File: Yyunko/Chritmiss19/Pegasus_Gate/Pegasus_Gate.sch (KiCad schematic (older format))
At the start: 38 parts, among them J1 Conn_01x03_Female, J2 Conn_01x03_Female, U1 WS2811, U2 WS2811, U3 WS2811, U4 1528-1537-ND

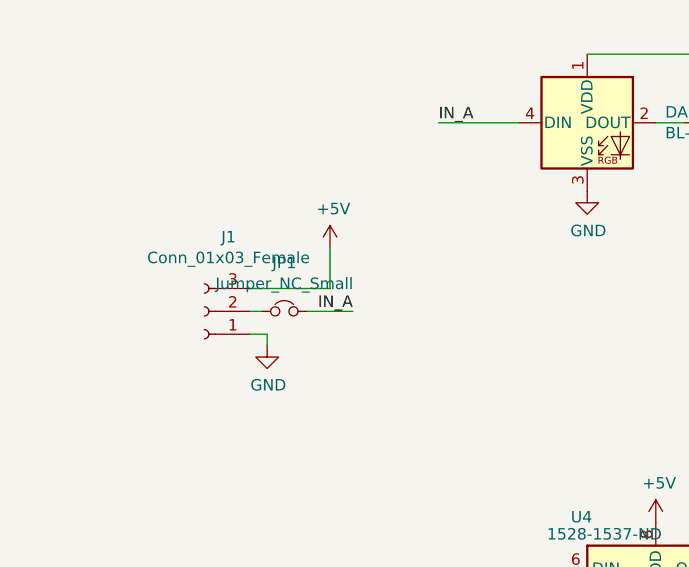
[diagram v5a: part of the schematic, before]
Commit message: Begin work on ESP32 code
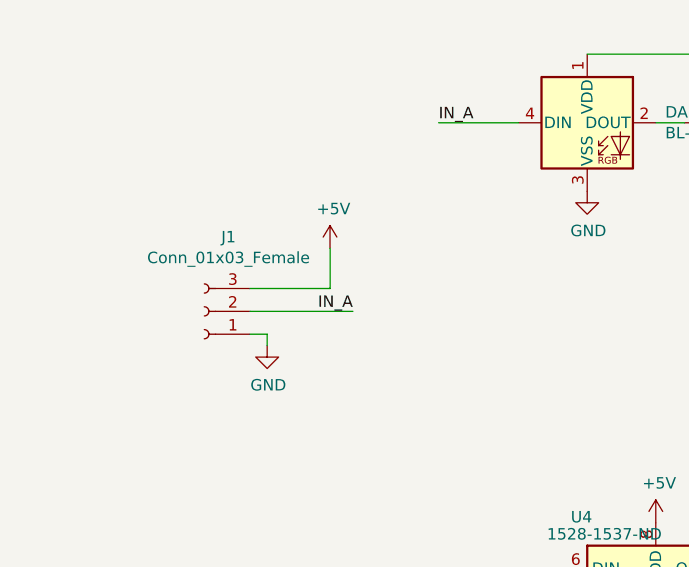
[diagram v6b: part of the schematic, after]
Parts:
- removed JP1: Jumper_NC_Small, Jumper:SolderJumper-2_P1.3mm_Bridged_Pad1.0x1.5mm, symbol Device:Jumper_NC_Small
- J1, J2: footprint Connector_PinHeader_2.00mm:PinHeader_1x03_P2.00mm_Vertical -> Connector_PinHeader_2.54mm:PinHeader_1x03_P2.54mm_Vertical
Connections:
- net IN_A: now also J1.2 (Pin_2)
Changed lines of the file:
@@
 F 0 "J1" H 3294 2050 50  0000 C CNN
 F 1 "Conn_01x03_Female" H 3294 2141 50  0000 C CNN
-F 2 "Connector_PinHeader_2.00mm:PinHeader_1x03_P2.00mm_Vertical" H 3400 2375 50  0001 C CNN
+F 2 "Connector_PinHeader_2.54mm:PinHeader_1x03_P2.54mm_Vertical" H 3400 2375 50  0001 C CNN
 F 3 "~" H 3400 2375 50  0001 C CNN
 	1    3400 2375
@@
 F 0 "J2" H 10169 2000 50  0000 C CNN
 F 1 "Conn_01x03_Female" H 10169 2091 50  0000 C CNN
-F 2 "Connector_PinHeader_2.00mm:PinHeader_1x03_P2.00mm_Vertical" H 10275 2325 50  0001 C CNN
+F 2 "Connector_PinHeader_2.54mm:PinHeader_1x03_P2.54mm_Vertical" H 10275 2325 50  0001 C CNN
 F 3 "~" H 10275 2325 50  0001 C CNN
 	1    10275 2325
@@
 	1    0    0    -1
 $EndComp
-$Comp
-L Device:Jumper_NC_Small JP1
-U 1 1 5DE11BC5
-P 3750 2375
-F 0 "JP1" H 3750 2587 50  0000 C CNN
-F 1 "Jumper_NC_Small" H 3750 2496 50  0000 C CNN
-F 2 "Jumper:SolderJumper-2_P1.3mm_Bridged_Pad1.0x1.5mm" H 3750 2375 50  0001 C CNN
-F 3 "~" H 3750 2375 50  0001 C CNN
-	1    3750 2375
-	1    0    0    -1
-$EndComp
-Wire Wire Line
-	3600 2375 3650 2375
-Wire Wire Line
-	3850 2375 4050 2375
 Wire Wire Line
 	4775 1550 4425 1550
@@
 	1    0    0    -1
 $EndComp
+Wire Wire Line
+	3600 2375 4050 2375
 $EndSCHEMATC
